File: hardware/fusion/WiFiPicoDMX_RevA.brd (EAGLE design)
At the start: 150 x 100 mm, 38 parts, among them J1 JST XH B4B-XH-A DMX: COM,-,+,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, J2 JST XH B5B-XH-A MIDI: 1,2,3,4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, J3 FREE GPIO PADS, J4 ANALOG PADS, J5 RESERVED SIGNAL TEST PADS, J6 POWER/DMX TEST PADS, SW1 PTS810SJM250SMTR LFS RESET (N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, U1 Raspberry Pi Pico 2 W, U2 ISOW1412DFMR, U3 HCPL-0700-500E

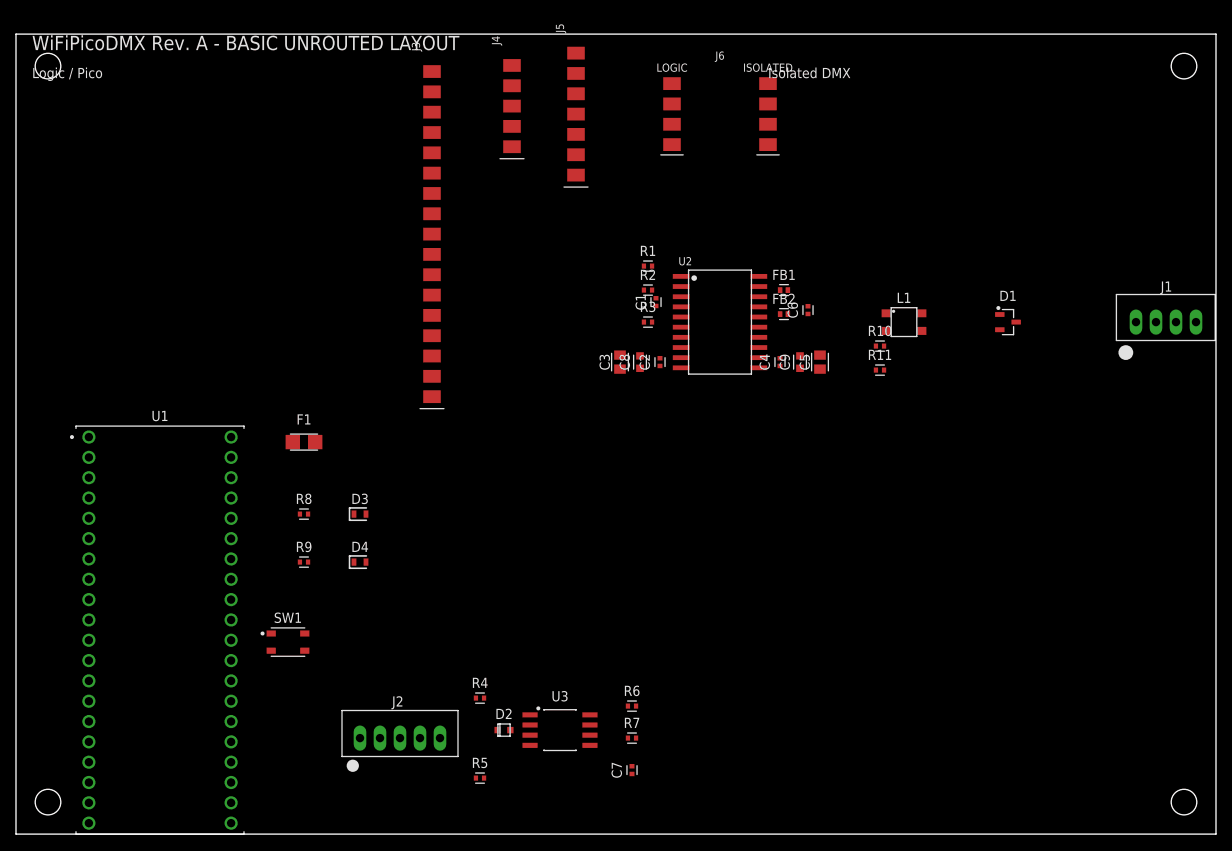
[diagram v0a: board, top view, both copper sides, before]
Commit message: hardware: reorganize board signal flow
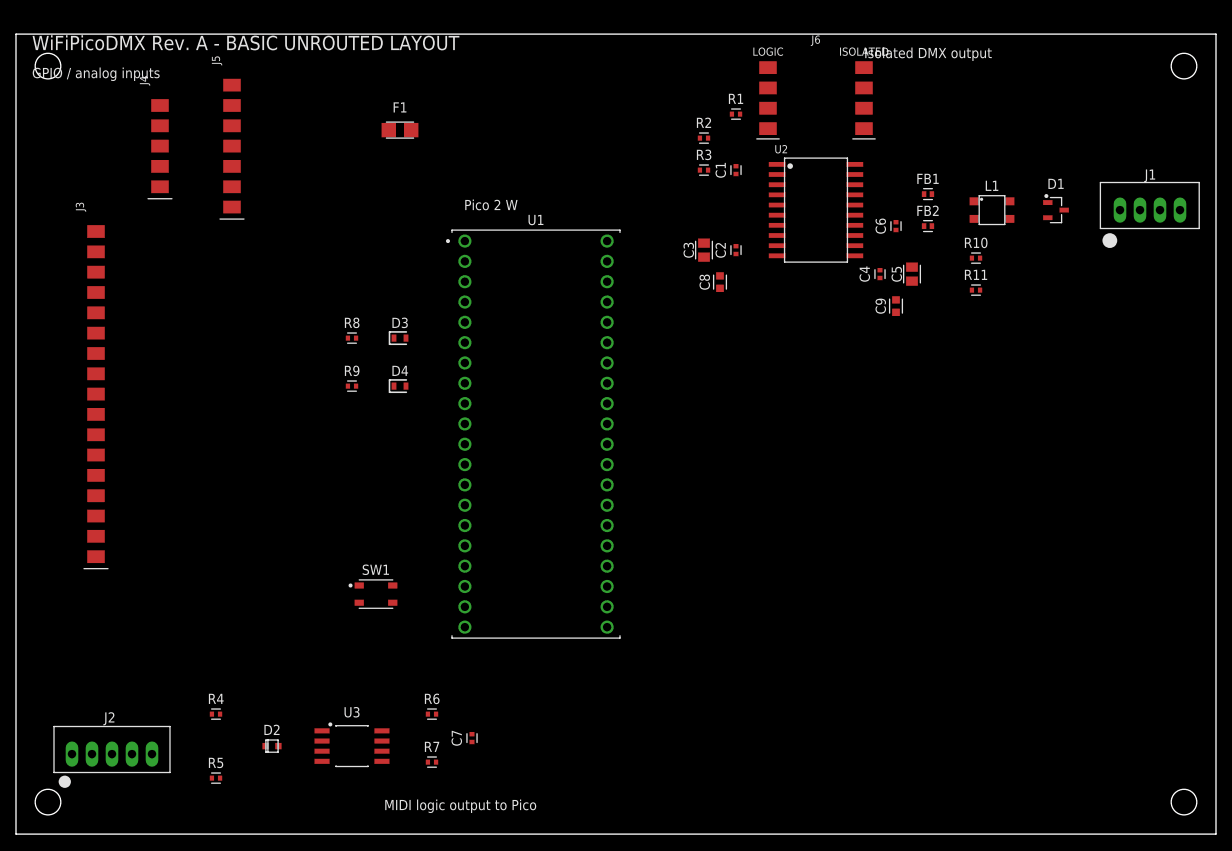
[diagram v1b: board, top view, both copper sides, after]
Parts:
- moved U1 53.0 mm to (65.0, 50.0)
- moved J3 46.5 mm to (10.0, 55.0)
- moved J4 44.3 mm to (18.0, 86.0)
- moved J5 43.2 mm to (27.0, 86.0)
- moved F1 40.8 mm to (48.0, 88.0)
- moved J2 36.1 mm to (12.0, 10.0)
- moved R4 33.1 mm to (25.0, 15.0)
- moved R5 33.0 mm to (25.0, 7.00)
- moved D2 29.1 mm to (32.0, 11.0)
- moved U3 26.1 mm to (42.0, 11.0)
- moved R7 25.2 mm to (52.0, 9.00)
- moved R6 25.0 mm to (52.0, 15.0)
- moved R8 22.8 mm to (42.0, 62.0)
- moved R9 22.8 mm to (42.0, 56.0)
- moved D3 22.6 mm to (48.0, 62.0)
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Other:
- board text added: "DMX ISOLATION - NO COPPER OR VIAS"
- board text added: "GPIO / analog inputs"
- board text added: "Isolated DMX output"
- board text added: "MIDI logic output to Pico"
- board text added: "Pico 2 W"
- board text removed: "ISOLATION CORRIDOR - NO COPPER OR VIAS"
- board text removed: "Isolated DMX"
- board text removed: "Logic / Pico"

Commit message: hardware: synchronize manual board placement
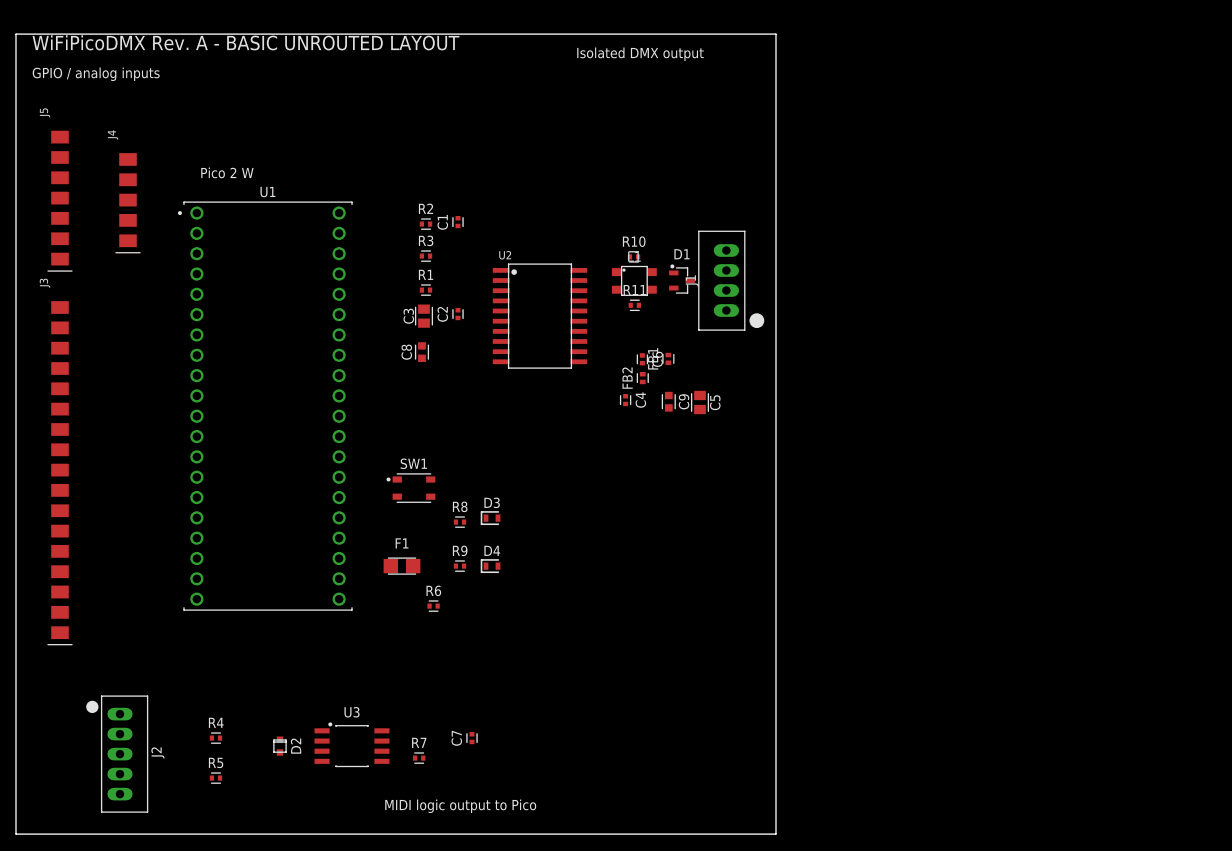
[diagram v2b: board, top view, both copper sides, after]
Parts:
- removed J6: POWER/DMX TEST PADS, WiFiPicoDMX_RevA_embedded:PADBANK8
- moved F1 54.5 mm to (48.2, 33.5)
- moved J1 50.8 mm to (88.8, 65.5), turned to 90 degrees
- moved D1 47.6 mm to (83.2, 69.2)
- moved L1 45.6 mm to (77.3, 69.2)
- moved R1 44.6 mm to (51.2, 68.0)
- moved R10 42.8 mm to (77.2, 72.2)
- moved R11 42.7 mm to (77.3, 66.1)
- moved FB2 40.4 mm to (78.3, 57.0), turned to 90 degrees
- moved FB1 38.4 mm to (81.5, 59.4), turned to 90 degrees
- moved C8 38.3 mm to (50.8, 60.2)
- moved U2 37.0 mm to (65.5, 64.8)
- moved R2 36.4 mm to (51.2, 76.2)
- moved R3 36.4 mm to (51.2, 72.2)
- moved C3 36.0 mm to (51.0, 64.8)
- moved C6 35.8 mm to (78.3, 59.4), turned to 270 degrees
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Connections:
- net DMX_DATA_MINUS: no longer J6.8
- net DMX_DATA_PLUS: no longer J6.7
- net GND_DMX_ISO: no longer J6.6
- net GND_LOGIC: no longer J6.2
- net VBUS_5V_USB: no longer J6.3
- net VCC_3V3_LOGIC: no longer J6.1
- net VCC_5V_DMX_ISO: no longer J6.5
- net VDD_5V_ISOW_FUSED: no longer J6.4
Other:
- board size 150 x 100 mm -> 95 x 100 mm
